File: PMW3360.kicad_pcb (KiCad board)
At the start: 2 copper layers, 40 x 15 mm, 10 parts, among them J1 Conn_01x07, U1 PMW3360, U2 TCR2EF19

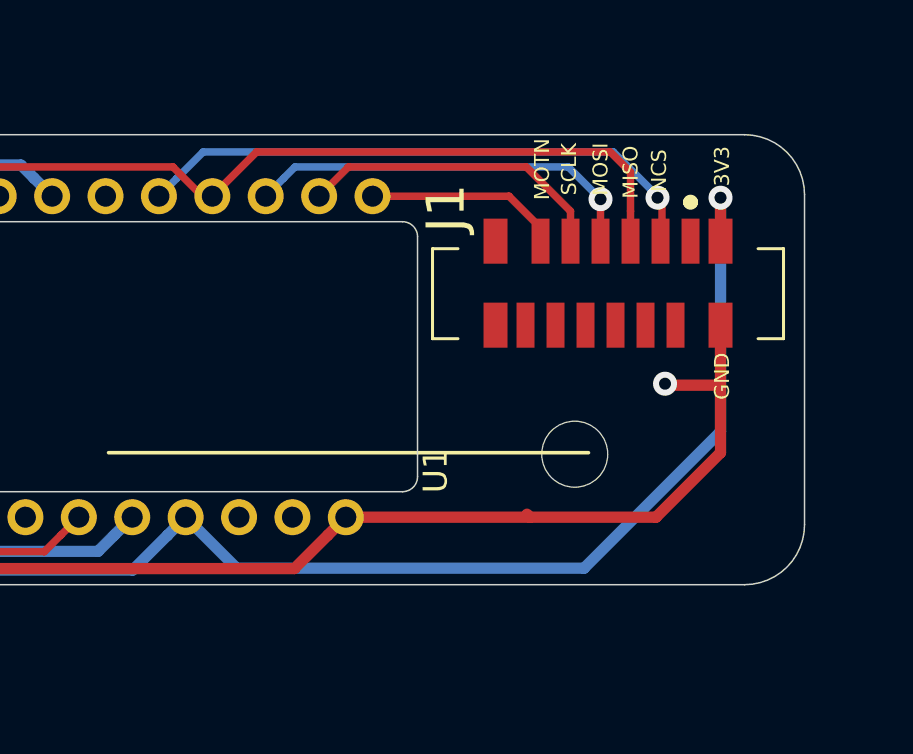
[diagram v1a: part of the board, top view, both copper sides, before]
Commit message: Corrected the power lines - connected them to the right pins of the sockets.
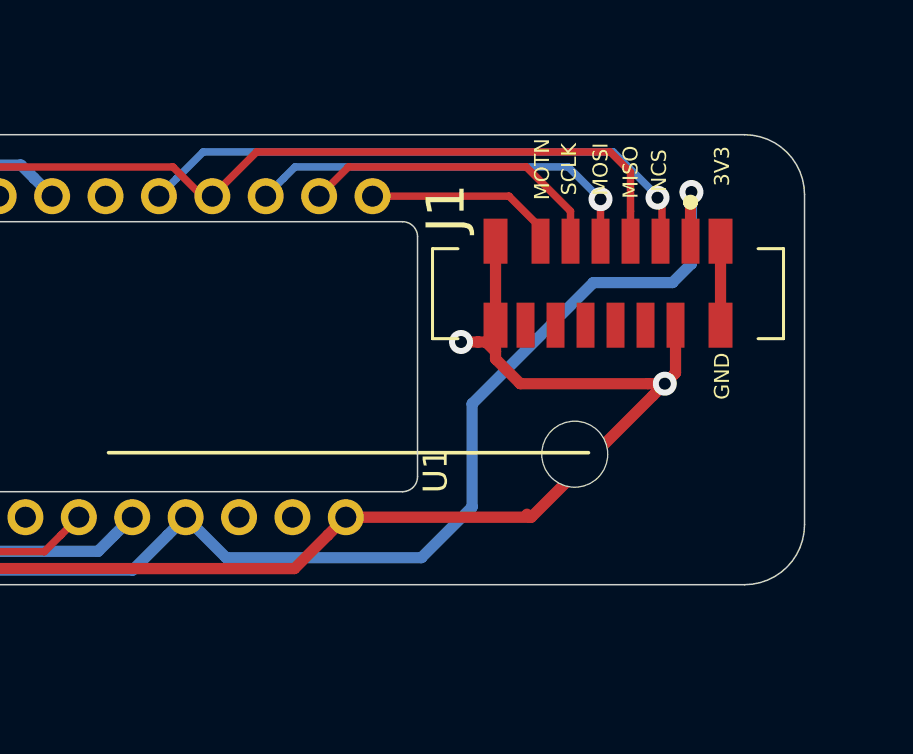
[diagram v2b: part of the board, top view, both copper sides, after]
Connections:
- J1 pad 1: (no net) -> +3V3
- J1 pad 2: (no net) -> GND
- J1 pad MP1: +3V3 -> GND
- J1 pad MP3: (no net) -> GND
- J1 pad MP4: (no net) -> GND
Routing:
- net GND: track 48.7 -> 57.8 mm, vias 3 -> 4
- net +3V3: track 57.6 -> 55.4 mm
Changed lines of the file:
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@@
   (general
     (thickness 1.6)
-    (drawings 33)
-    (tracks 111)
+    (drawings 34)
+    (tracks 126)
     (zones 0)
     (modules 10)
@@
     (pad_to_mask_clearance 0)
     (aux_axis_origin 0 0)
-    (grid_origin 171.95 108.05)
+    (grid_origin 170.81 100.98)
     (visible_elements 7FFFFFFF)
     (pcbplotparams
@@
       (drillshape 0)
       (scaleselection 1)
-      (outputdirectory "./"))
+      (outputdirectory "Fabrication/"))
   )
   (net 0 "")
@@
     (add_net NCS)
     (add_net "Net-(C3-Pad1)")
+    (add_net "Net-(J1-Pad10)")
+    (add_net "Net-(J1-Pad12)")
+    (add_net "Net-(J1-Pad4)")
+    (add_net "Net-(J1-Pad6)")
+    (add_net "Net-(J1-Pad8)")
+    (add_net "Net-(U1-Pad1)")
+    (add_net "Net-(U1-Pad14)")
+    (add_net "Net-(U1-Pad16)")
+    (add_net "Net-(U1-Pad2)")
+    (add_net "Net-(U1-Pad6)")
+    (add_net "Net-(U1-Pad7)")
+    (add_net "Net-(U2-Pad4)")
     (add_net SCLK)
   )
@@
     (fp_line (start 5.85 -1.85) (end 5.85 1.15) (layer Dwgs.User) (width 0.2))
     (fp_line (start -5.85 -1.85) (end 5.85 -1.85) (layer Dwgs.User) (width 0.2))
-    (pad MP4 smd rect (at 3.75 -1.4 180) (size 0.8 1.5) (layers F.Cu F.Paste F.Mask))
-    (pad MP3 smd rect (at 3.75 1.4 180) (size 0.8 1.5) (layers F.Cu F.Paste F.Mask))
+    (pad MP4 smd rect (at 3.75 -1.4 180) (size 0.8 1.5) (layers F.Cu F.Paste F.Mask)
+      (net 2 GND))
+    (pad MP3 smd rect (at 3.75 1.4 180) (size 0.8 1.5) (layers F.Cu F.Paste F.Mask)
+      (net 2 GND))
     (pad MP2 smd rect (at -3.75 -1.4 180) (size 0.8 1.5) (layers F.Cu F.Paste F.Mask)
       (net 2 GND))
     (pad MP1 smd rect (at -3.75 1.4 180) (size 0.8 1.5) (layers F.Cu F.Paste F.Mask)
-      (net 1 +3V3))
+      (net 2 GND))
     (pad 12 smd rect (at 2.75 -1.4 180) (size 0.6 1.5) (layers F.Cu F.Paste F.Mask))
     (pad 11 smd rect (at 2.25 1.4 180) (size 0.6 1.5) (layers F.Cu F.Paste F.Mask)
@@
     (pad 3 smd rect (at -1.75 1.4 180) (size 0.6 1.5) (layers F.Cu F.Paste F.Mask)
       (net 9 NCS))
-    (pad 2 smd rect (at -2.25 -1.4 180) (size 0.6 1.5) (layers F.Cu F.Paste F.Mask))
-    (pad 1 smd rect (at -2.75 1.4 180) (size 0.6 1.5) (layers F.Cu F.Paste F.Mask))
+    (pad 2 smd rect (at -2.25 -1.4 180) (size 0.6 1.5) (layers F.Cu F.Paste F.Mask)
+      (net 2 GND))
+    (pad 1 smd rect (at -2.75 1.4 180) (size 0.6 1.5) (layers F.Cu F.Paste F.Mask)
+      (net 1 +3V3))
   )
   (module PMW3360:PMW3360 locked (layer F.Cu)
@@
     )
   )
+  (dimension 7.39 (width 0.12) (layer F.SilkS)
+    (gr_text "7.390 mm" (at 163.08 101.145 90) (layer F.SilkS)
+      (effects (font (size 1 1) (thickness 0.15)))
+    )
+    (feature1 (pts (xy 159.08 97.45) (xy 162.396421 97.45)))
+    (feature2 (pts (xy 159.08 104.84) (xy 162.396421 104.84)))
+    (crossbar (pts (xy 161.81 104.84) (xy 161.81 97.45)))
+    (arrow1a (pts (xy 161.81 97.45) (xy 162.396421 98.576504)))
+    (arrow1b (pts (xy 161.81 97.45) (xy 161.223579 98.576504)))
+    (arrow2a (pts (xy 161.81 104.84) (xy 162.396421 103.713496)))
+    (arrow2b (pts (xy 161.81 104.84) (xy 161.223579 103.713496)))
+  )
   (dimension 3.2 (width 0.12) (layer F.SilkS)
     (gr_text "3.200 mm" (at 154.75 106.46 270) (layer F.SilkS)
@@
   (segment (start 147.15 104.7) (end 147.05 104.6) (width 0.375) (layer B.Cu) (net 1))
   (segment (start 147.15 108.85) (end 147.15 104.7) (width 0.375) (layer B.Cu) (net 1))
-  (via (at 178.35 99.55) (size 0.8) (drill 0.4) (layers F.Cu B.Cu) (net 1))
-  (segment (start 178.35 101) (end 178.35 99.55) (width 0.375) (layer F.Cu) (net 1))
-  (segment (start 178.35 107.35) (end 178.35 99.55) (width 0.375) (layer B.Cu) (net 1))
-  (segment (start 173.8 111.9) (end 178.35 107.35) (width 0.375) (layer B.Cu) (net 1))
-  (segment (start 160.52 110.2) (end 162.22 111.9) (width 0.375) (layer B.Cu) (net 1))
-  (segment (start 162.22 111.9) (end 173.8 111.9) (width 0.375) (layer B.Cu) (net 1))
   (segment (start 159.920001 110.799999) (end 160.52 110.2) (width 0.375) (layer B.Cu) (net 1))
   (segment (start 158.757489 111.962511) (end 159.920001 110.799999) (width 0.375) (layer B.Cu) (net 1))
@@
   (segment (start 147.05 104.6) (end 147.05 101.35) (width 0.375) (layer F.Cu) (net 1))
   (segment (start 147.05 101.35) (end 147.95 100.45) (width 0.375) (layer F.Cu) (net 1))
+  (via (at 177.380002 99.36) (size 0.8) (drill 0.4) (layers F.Cu B.Cu) (net 1))
+  (segment (start 177.35 101) (end 177.35 99.390002) (width 0.375) (layer F.Cu) (net 1))
+  (segment (start 177.35 99.390002) (end 177.380002 99.36) (width 0.375) (layer F.Cu) (net 1))
+  (segment (start 177.380002 101.749998) (end 177.380002 99.36) (width 0.375) (layer B.Cu) (net 1))
+  (segment (start 161.87 111.55) (end 168.38 111.55) (width 0.375) (layer B.Cu) (net 1))
+  (segment (start 160.52 110.2) (end 161.87 111.55) (width 0.375) (layer B.Cu) (net 1))
+  (segment (start 176.75 102.38) (end 177.380002 101.749998) (width 0.375) (layer B.Cu) (net 1))
+  (segment (start 168.38 111.55) (end 170.07 109.86) (width 0.375) (layer B.Cu) (net 1))
+  (segment (start 170.07 106.42) (end 174.11 102.38) (width 0.375) (layer B.Cu) (net 1))
+  (segment (start 170.07 109.86) (end 170.07 106.42) (width 0.375) (layer B.Cu) (net 1))
+  (segment (start 174.11 102.38) (end 176.75 102.38) (width 0.375) (layer B.Cu) (net 1))
   (segment (start 147.255 106.25) (end 148.16 106.25) (width 0.375) (layer F.Cu) (net 2))
   (via (at 148.16 106.25) (size 0.8) (drill 0.4) (layers F.Cu B.Cu) (net 2))
@@
   (segment (start 148 104.402498) (end 148.222501 104.624999) (width 0.375) (layer F.Cu) (net 2))
   (segment (start 148 103.6) (end 148 104.402498) (width 0.375) (layer F.Cu) (net 2))
-  (segment (start 176.2 110.2) (end 178.35 108.05) (width 0.375) (layer F.Cu) (net 2))
   (segment (start 165.86 110.2) (end 172 110.2) (width 0.375) (layer F.Cu) (net 2))
-  (segment (start 172 110.2) (end 176.2 110.2) (width 0.375) (layer F.Cu) (net 2))
   (segment (start 149.083306 108.433306) (end 149.55 108.9) (width 0.375) (layer F.Cu) (net 2))
   (segment (start 148.3 107.65) (end 149.083306 108.433306) (width 0.375) (layer F.Cu) (net 2))
   (segment (start 148.16 106.25) (end 148.3 106.39) (width 0.375) (layer F.Cu) (net 2))
   (segment (start 148.3 106.39) (end 148.3 107.65) (width 0.375) (layer F.Cu) (net 2))
-  (via (at 176.5 105.75) (size 0.8) (drill 0.4) (layers F.Cu B.Cu) (net 2))
-  (segment (start 176.55 105.8) (end 176.5 105.75) (width 0.375) (layer F.Cu) (net 2))
-  (segment (start 178.35 105.8) (end 176.55 105.8) (width 0.375) (layer F.Cu) (net 2))
-  (segment (start 178.35 105.8) (end 178.35 103.8) (width 0.375) (layer F.Cu) (net 2))
-  (segment (start 178.35 108.05) (end 178.35 105.8) (width 0.375) (layer F.Cu) (net 2))
   (segment (start 165.260001 110.799999) (end 165.86 110.2) (width 0.375) (layer F.Cu) (net 2))
   (segment (start 164.14749 111.91251) (end 165.260001 110.799999) (width 0.375) (layer F.Cu) (net 2))
@@
   (segment (start 148 110.45) (end 148.95 111.4) (width 0.375) (layer F.Cu) (net 2))
   (segment (start 171.9 110.1) (end 172 110.2) (width 0.375) (layer F.Cu) (net 2))
+  (segment (start 170.85 101) (end 170.85 103.8) (width 0.375) (layer F.Cu) (net 2))
+  (segment (start 178.35 101) (end 178.35 103.8) (width 0.375) (layer F.Cu) (net 2))
+  (via (at 176.49249 105.75) (size 0.8) (drill 0.4) (layers F.Cu B.Cu) (net 2))
+  (segment (start 170.85 104.925) (end 171.675 105.75) (width 0.375) (layer F.Cu) (net 2))
+  (segment (start 172 110.2) (end 172.04249 110.2) (width 0.375) (layer F.Cu) (net 2))
+  (segment (start 171.675 105.75) (end 175.926805 105.75) (width 0.375) (layer F.Cu) (net 2))
+  (segment (start 176.85 105.39249) (end 176.49249 105.75) (width 0.375) (layer F.Cu) (net 2))
+  (segment (start 175.926805 105.75) (end 176.49249 105.75) (width 0.375) (layer F.Cu) (net 2))
+  (segment (start 176.85 103.8) (end 176.85 105.39249) (width 0.375) (layer F.Cu) (net 2))
+  (segment (start 176.092491 106.149999) (end 176.49249 105.75) (width 0.375) (layer F.Cu) (net 2))
+  (segment (start 172.04249 110.2) (end 176.092491 106.149999) (width 0.375) (layer F.Cu) (net 2))
+  (segment (start 170.85 104.68) (end 170.85 104.925) (width 0.375) (layer F.Cu) (net 2))
+  (segment (start 170.85 103.8) (end 170.85 104.68) (width 0.375) (layer F.Cu) (net 2))
+  (via (at 169.7 104.359998) (size 0.8) (drill 0.4) (layers F.Cu B.Cu) (net 2))
+  (segment (start 170.85 104.68) (end 170.529998 104.359998) (width 0.375) (layer F.Cu) (net 2))
+  (segment (start 170.265685 104.359998) (end 169.7 104.359998) (width 0.375) (layer F.Cu) (net 2))
+  (segment (start 170.529998 104.359998) (end 170.265685 104.359998) (width 0.375) (layer F.Cu) (net 2))
   (via (at 149.45 105.95) (size 0.8) (drill 0.4) (layers F.Cu B.Cu) (net 3))
   (segment (start 149.455 105.3) (end 149.455 105.945) (width 0.375) (layer F.Cu) (net 3))
